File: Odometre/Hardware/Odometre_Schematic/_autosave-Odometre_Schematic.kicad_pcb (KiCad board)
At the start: 2 copper layers, 83.2 x 61.6 mm, 35 parts, among them IC1 STM32C092FCP6, J1 Conn_01x03_Pin, J2 Conn_01x03_Pin, J3 Conn_Alim, J4 Conn_Laser1, J5 Conn_Laser2, J6 Conn_SWD, J7 Conn_01x06_Pin, U1 MCP2562-E-SN, U2 LM1117DT-3.3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

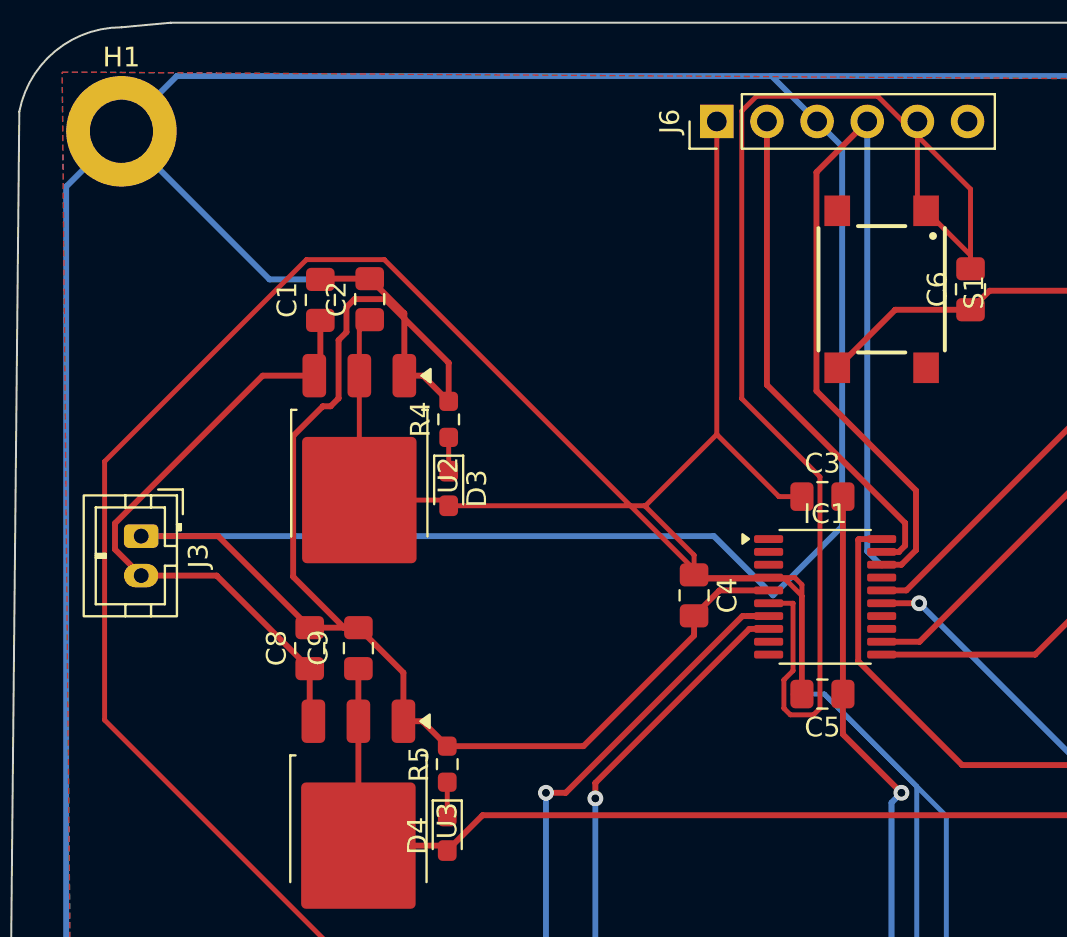
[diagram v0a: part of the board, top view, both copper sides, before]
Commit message: routage du pcb
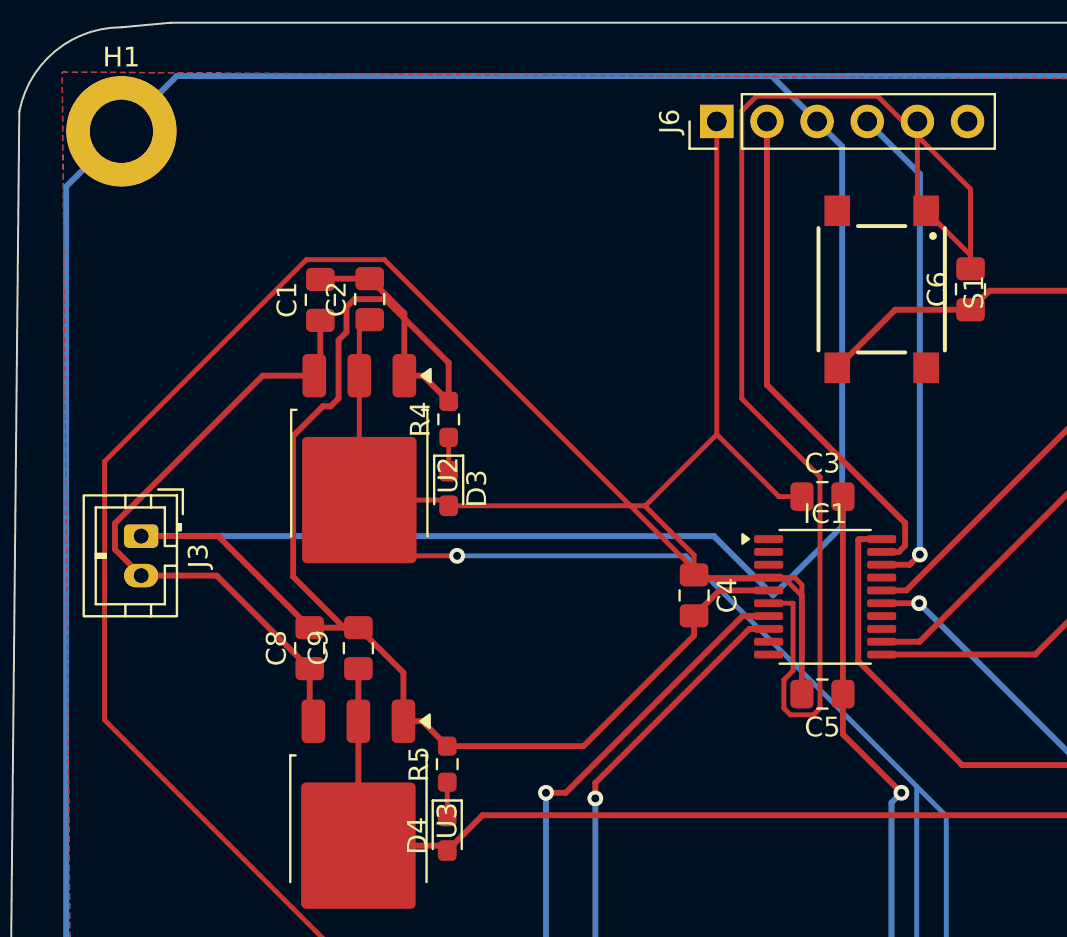
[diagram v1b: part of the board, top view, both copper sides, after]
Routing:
- net DEBUG_SWDIO: track 49.7 -> 25.2 mm, vias 0 -> 1
- net VDD/VDDA: track 271.8 -> 291.2 mm, vias 0 -> 1
- net GND: track 552.9 -> 539.3 mm
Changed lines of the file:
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@@
-	)
-	(segment
-		(start 124.5 72)
-		(end 127.5 72)
-		(width 0.3)
-		(layer "B.Cu")
-		(net 2)
 	)
 	(segment
@@
 	)
 	(segment
-		(start 117 64.5)
-		(end 124.5 72)
-		(width 0.3)
-		(layer "B.Cu")
-		(net 2)
-	)
-	(segment
 		(start 149.930001 61.700001)
 		(end 152.23 64)
@@
 	)
 	(segment
+		(start 131.8725 86)
+		(end 129.0475 83.175)
+		(width 0.25)
+		(layer "F.Cu")
+		(net 3)
+	)
+	(segment
 		(start 130.666774 108.834)
 		(end 133.537272 108.834)
@@
 	)
 	(segment
+		(start 134 86)
+		(end 131.8725 86)
+		(width 0.25)
+		(layer "F.Cu")
+		(net 3)
+	)
+	(segment
 		(start 147.15 79.85)
 		(end 143.51875 83.48125)
@@
 		(net 3)
 	)
-	(segment
-		(start 157.276 97.67857)
-		(end 152.59743 93)
-		(width 0.25)
-		(layer "B.Cu")
-		(net 3)
-	)
-	(segment
-		(start 152.59743 93)
-		(end 158.774 99.17657)
+	(via
+		(at 134 86)
+		(size 0.8)
+		(drill 0.4)
+		(layers "F.Cu" "B.Cu")
+		(net 3)
+	)
+	(segment
+		(start 156.507826 111.686)
+		(end 157.276 110.917826)
 		(width 0.25)
 		(layer "B.Cu")
@@
 	)
 	(segment
+		(start 145.314 111.686)
+		(end 156.507826 111.686)
+		(width 0.25)
+		(layer "B.Cu")
+		(net 3)
+	)
+	(segment
+		(start 158.774 99.17657)
+		(end 158.774 111.055826)
+		(width 0.25)
+		(layer "B.Cu")
+		(net 3)
+	)
+	(segment
+		(start 145.59743 86)
+		(end 134 86)
+		(width 0.25)
+		(layer "B.Cu")
+		(net 3)
+	)
+	(segment
+		(start 161.226 112.492174)
+		(end 161.226 114.314)
+		(width 0.25)
+		(layer "B.Cu")
+		(net 3)
+	)
+	(segment
+		(start 157.276 110.917826)
+		(end 157.276 97.67857)
+		(width 0.25)
+		(layer "B.Cu")
+		(net 3)
+	)
+	(segment
 		(start 143 114)
 		(end 145.314 111.686)
@@
 	)
 	(segment
-		(start 158.774 99.17657)
-		(end 158.774 111.055826)
-		(width 0.25)
-		(layer "B.Cu")
-		(net 3)
-	)
-	(segment
-		(start 157.276 110.917826)
-		(end 157.276 97.67857)
-		(width 0.25)
-		(layer "B.Cu")
-		(net 3)
-	)
-	(segment
-		(start 152.59743 93)
-		(end 151 93)
-		(width 0.25)
-		(layer "B.Cu")
-		(net 3)
-	)
-	(segment
-		(start 161.226 112.492174)
-		(end 161.226 114.314)
-		(width 0.25)
-		(layer "B.Cu")
-		(net 3)
-	)
-	(segment
-		(start 156.507826 111.686)
-		(end 157.276 110.917826)
-		(width 0.25)
-		(layer "B.Cu")
-		(net 3)
-	)
-	(segment
 		(start 143 114)
 		(end 144.54 115.54)
@@
 	)
 	(segment
-		(start 145.314 111.686)
-		(end 156.507826 111.686)
+		(start 158.774 99.17657)
+		(end 145.59743 86)
 		(width 0.25)
 		(layer "B.Cu")
@@
 	)
 	(segment
-		(start 156.498736 86.45)
-		(end 157.2395 85.709236)
+		(start 156.918628 86.45)
+		(end 155.5 86.45)
 		(width 0.3)
 		(layer "F.Cu")
@@
 	)
 	(segment
-		(start 157.2395 85.709236)
-		(end 157.2395 82.6915)
+		(start 157.434314 85.934314)
+		(end 156.918628 86.45)
 		(width 0.3)
 		(layer "F.Cu")
 		(net 13)
 	)
-	(segment
-		(start 155.5 86.45)
-		(end 156.498736 86.45)
-		(width 0.3)
-		(layer "F.Cu")
+	(via
+		(at 157.434314 85.934314)
+		(size 0.8)
+		(drill 0.4)
+		(layers "F.Cu" "B.Cu")
 		(net 13)
 	)
 	(segment
-		(start 152.199 77.651)
-		(end 152.199 66.571)
-		(width 0.3)
-		(layer "F.Cu")
+		(start 157.434314 66.664314)
+		(end 157.434314 85.934314)
+		(width 0.3)
+		(layer "B.Cu")
 		(net 13)
 	)
 	(segment
-		(start 157.2395 82.6915)
-		(end 152.199 77.651)
-		(width 0.3)
-		(layer "F.Cu")
-		(net 13)
-	)
-	(segment
-		(start 152.199 66.571)
-		(end 154.77 64)
-		(width 0.3)
-		(layer "F.Cu")
-		(net 13)
-	)
-	(segment
-		(start 154.77 85.77)
-		(end 155.5 86.5)
-		(width 0.3)
-		(layer "B.Cu")
-		(net 13)
-	)
-	(segment
 		(start 154.77 64)
-		(end 154.77 85.77)
-		(width 0.3)
-		(layer "B.Cu")
+		(end 157.434314 66.664314)
+		(width 0.3)
+		(layer "B.Cu")

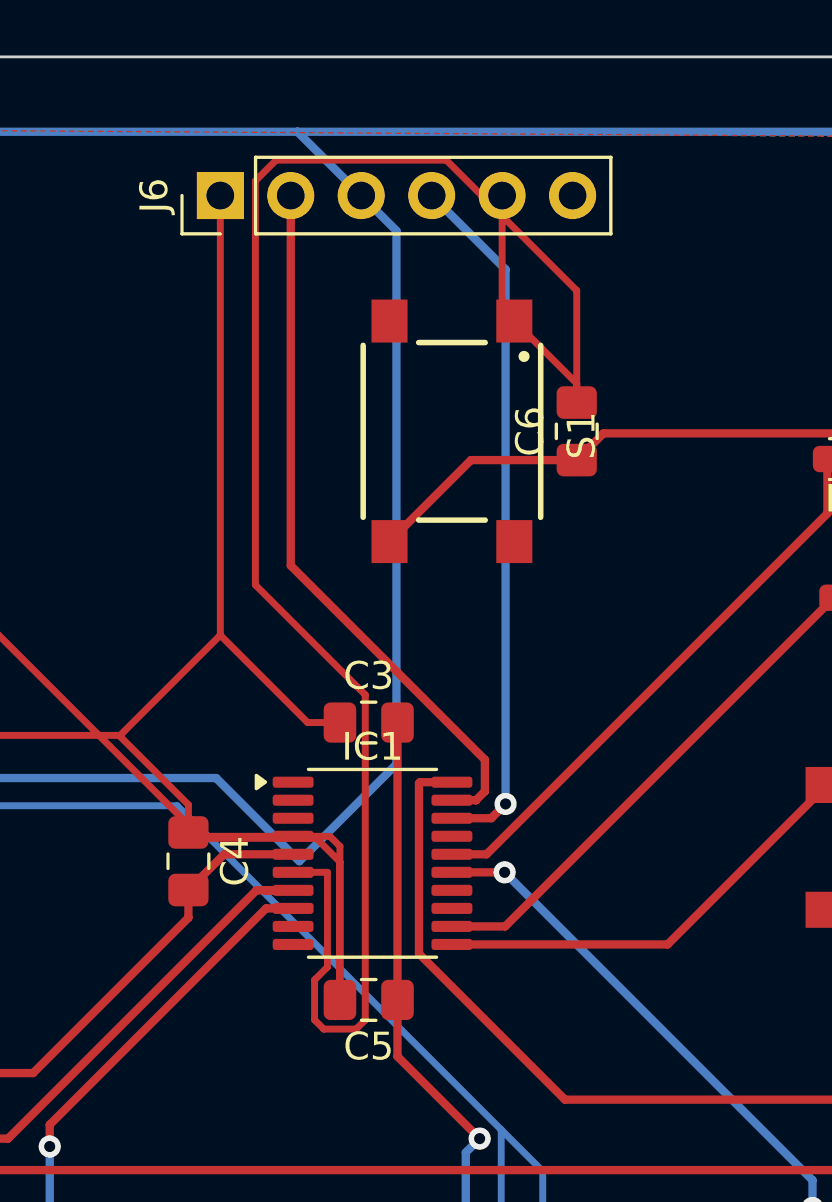
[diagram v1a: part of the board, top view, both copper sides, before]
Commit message: modif d'empreintes
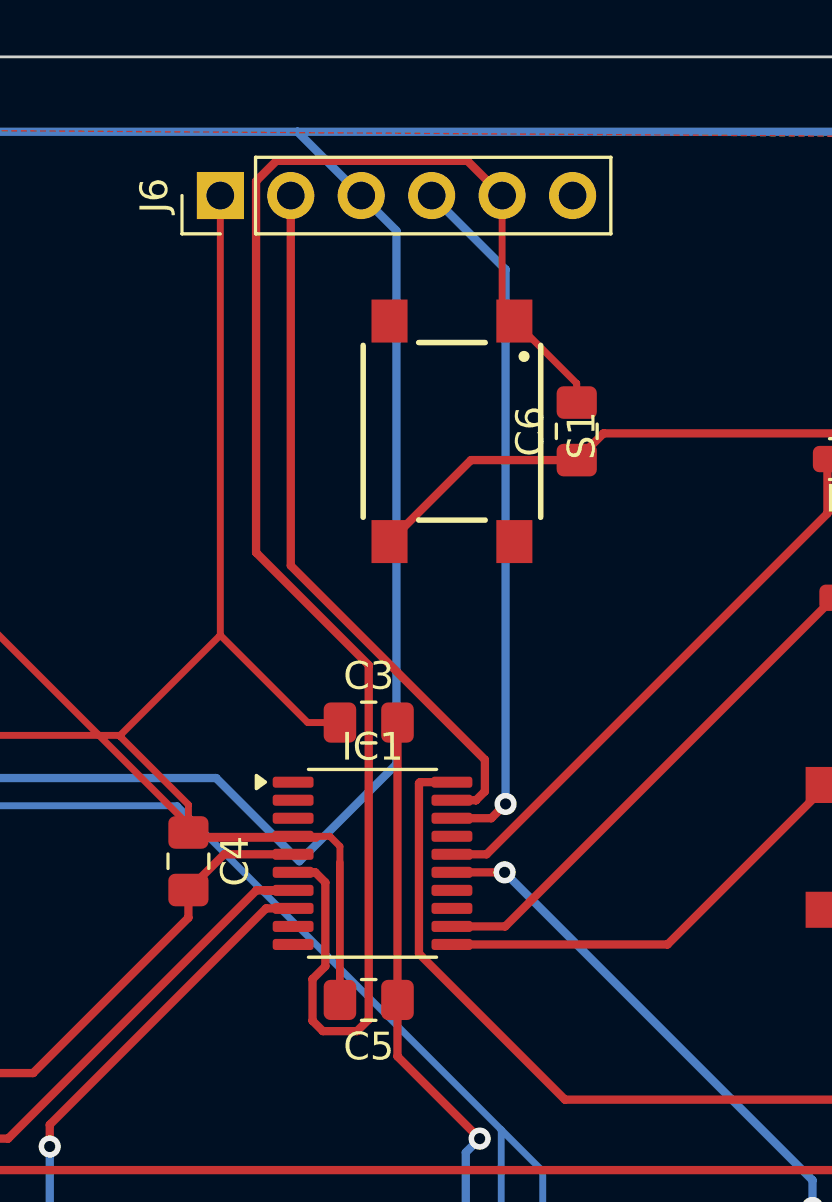
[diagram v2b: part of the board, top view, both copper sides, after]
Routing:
- net NRST: track 67.2 -> 59.0 mm
- net VDD/VDDA: track 291.2 -> 290.0 mm
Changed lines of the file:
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@@
-	)
-	(segment
-		(start 151.4625 88.024062)
-		(end 150.612438 87.174)
-		(width 0.25)
-		(layer "F.Cu")
-		(net 3)
 	)
 	(segment
@@
 	)
 	(segment
-		(start 149.161463 62.724)
-		(end 155.298537 62.724)
-		(width 0.25)
-		(layer "F.Cu")
-		(net 4)
-	)
-	(segment
-		(start 160 67.425463)
-		(end 160 71.4625)
-		(width 0.25)
-		(layer "F.Cu")
-		(net 4)
-	)
-	(segment
-		(start 152.376 82)
-		(end 148.414 78.038)
-		(width 0.25)
-		(layer "F.Cu")
-		(net 4)
-	)
-	(segment
-		(start 155.298537 62.724)
-		(end 160 67.425463)
-		(width 0.25)
-		(layer "F.Cu")
-		(net 4)
-	)
-	(segment
-		(start 148.414 63.471463)
-		(end 149.161463 62.724)
-		(width 0.25)
+		(start 149.171818 62.749)
+		(end 156.059 62.749)
+		(width 0.3)
+		(layer "F.Cu")
+		(net 4)
+	)
+	(segment
+		(start 150.474 92.24842)
+		(end 150.474 93.75158)
+		(width 0.3)
 		(layer "F.Cu")
 		(net 4)
@@
 	)
 	(segment
-		(start 152.376 93.720514)
-		(end 152.376 82)
-		(width 0.25)
+		(start 148.439 76.86994)
+		(end 148.439 63.481818)
+		(width 0.3)
 		(layer "F.Cu")
 		(net 4)
@@
 	)
 	(segment
-		(start 150.549 92.279486)
-		(end 150.549 93.720514)
-		(width 0.25)
-		(layer "F.Cu")
-		(net 4)
-	)
-	(segment
-		(start 151.0115 91.816986)
-		(end 150.549 92.279486)
-		(width 0.25)
-		(layer "F.Cu")
-		(net 4)
-	)
-	(segment
-		(start 151.0115 88.4)
-		(end 151.0115 91.816986)
-		(width 0.25)
+		(start 152.5 93.70258)
+		(end 152.5 80.93094)
+		(width 0.3)
+		(layer "F.Cu")
+		(net 4)
+	)
+	(segment
+		(start 150.84842 94.126)
+		(end 152.07658 94.126)
+		(width 0.3)
+		(layer "F.Cu")
+		(net 4)
+	)
+	(segment
+		(start 148.439 63.481818)
+		(end 149.171818 62.749)
+		(width 0.3)
+		(layer "F.Cu")
+		(net 4)
+	)
+	(segment
+		(start 149.775 88.4)
+		(end 150.573792 88.4)
+		(width 0.3)
+		(layer "F.Cu")
+		(net 4)
+	)
+	(segment
+		(start 152.5 80.93094)
+		(end 148.439 76.86994)
+		(width 0.3)
 		(layer "F.Cu")
 		(net 4)
@@
 	)
 	(segment
-		(start 150.549 93.720514)
-		(end 150.879486 94.051)
-		(width 0.25)
-		(layer "F.Cu")
-		(net 4)
-	)
-	(segment
-		(start 150.879486 94.051)
-		(end 152.045514 94.051)
-		(width 0.25)
-		(layer "F.Cu")
-		(net 4)
-	)
-	(segment
-		(start 149.775 88.4)
-		(end 151.0115 88.4)
-		(width 0.25)
-		(layer "F.Cu")
-		(net 4)
-	)
-	(segment
-		(start 148.414 78.038)
-		(end 148.414 63.471463)
-		(width 0.25)
+		(start 156.059 62.749)
+		(end 157.31 64)
+		(width 0.3)
+		(layer "F.Cu")
+		(net 4)
+	)
+	(segment
+		(start 150.9365 88.762708)
+		(end 150.9365 91.78592)
+		(width 0.3)
+		(layer "F.Cu")
+		(net 4)
+	)
+	(segment
+		(start 152.07658 94.126)
+		(end 152.5 93.70258)
+		(width 0.3)
 		(layer "F.Cu")
 		(net 4)
@@
 	)
 	(segment
-		(start 152.045514 94.051)
-		(end 152.376 93.720514)
-		(width 0.25)
-		(layer "F.Cu")
-		(net 4)
+		(start 150.9365 91.78592)
+		(end 150.474 92.24842)
+		(width 0.3)
+		(layer "F.Cu")
+		(net 4)
+	)
+	(segment
+		(start 150.474 93.75158)
+		(end 150.84842 94.126)
+		(width 0.3)
+		(layer "F.Cu")
+		(net 4)
+	)
+	(segment
+		(start 150.573792 88.4)
+		(end 150.9365 88.762708)
+		(width 0.3)
+		(layer "F.Cu")
+		(net 4)
